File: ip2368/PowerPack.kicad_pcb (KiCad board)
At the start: 2 copper layers, 79 x 31 mm, 75 parts, among them CN1 XT30PW-M, Q1 WSD3066DN33, U1 IP2368_BZ_VGLIP_C5203723, U2 ME6203A50PG

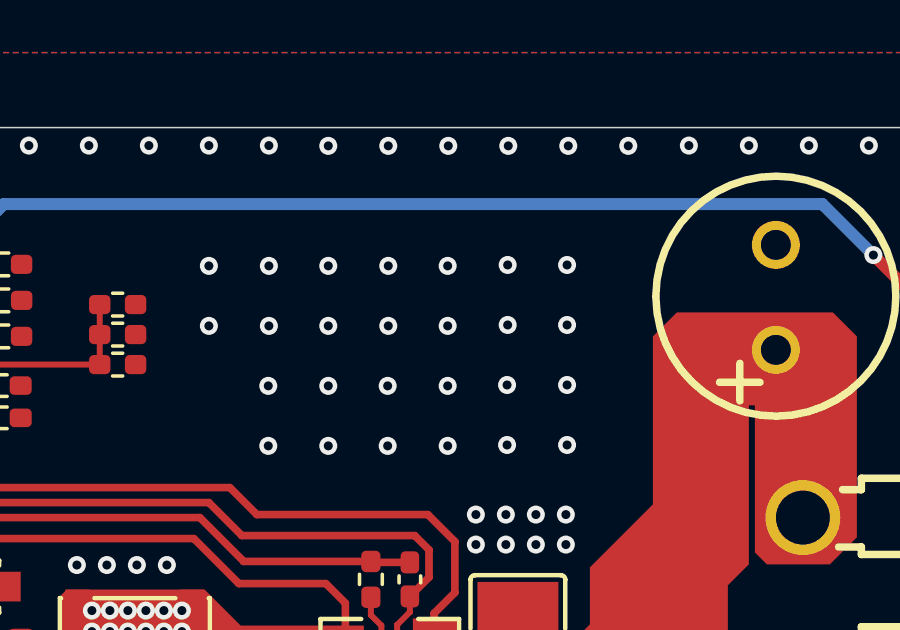
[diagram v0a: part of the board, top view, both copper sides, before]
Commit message: add logo
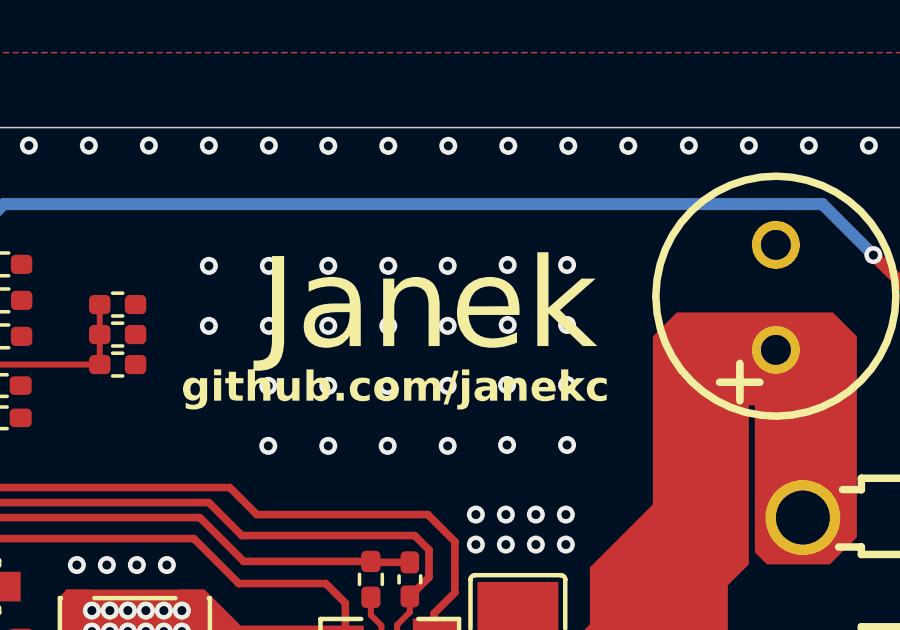
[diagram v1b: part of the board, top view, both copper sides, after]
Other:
- board text added: "Janek"
- board text added: "github.com/janekc"
